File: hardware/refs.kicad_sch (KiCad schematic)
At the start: 26 parts, among them U4 LM4040DBZ-4.1, U5 OPA4991, U6 OPA4991

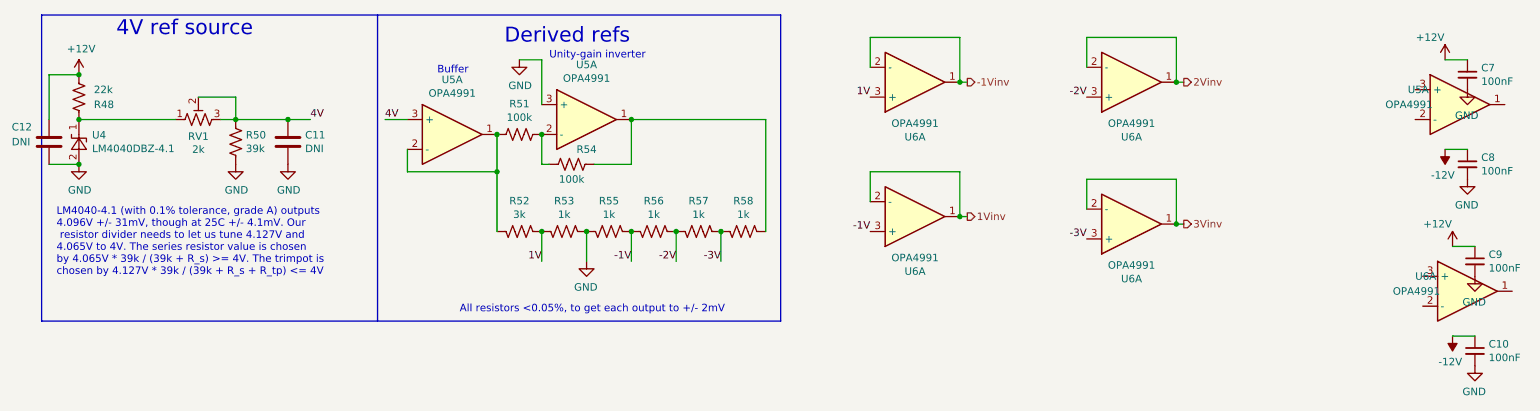
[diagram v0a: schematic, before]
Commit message: Fix 3d models and migrate to KiCad6 R/C footprints
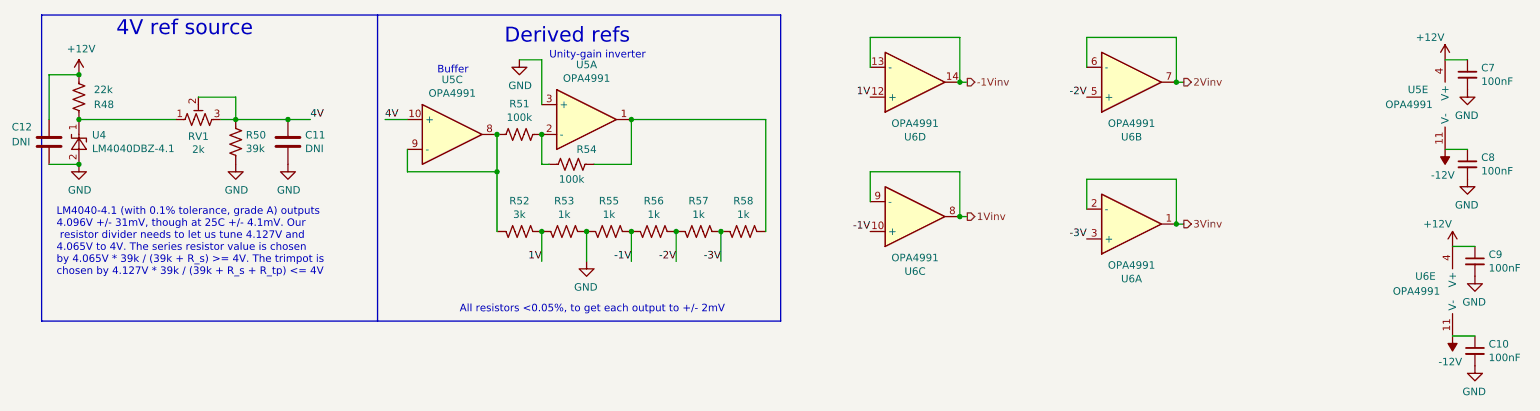
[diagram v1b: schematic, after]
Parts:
- C10, C11, C12, C7, C8, C9: footprint Capacitor_SMD:C_0603_1608Metric_Pad1.05x0.95mm_HandSolder -> Capacitor_SMD:C_0603_1608Metric_Pad1.08x0.95mm_HandSolder
- R48, R50, R51, R52, R53, R54, R55, R56, R57, R58: footprint Resistor_SMD:R_0603_1608Metric_Pad1.05x0.95mm_HandSolder -> Resistor_SMD:R_0603_1608Metric_Pad0.98x0.95mm_HandSolder
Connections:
- net +12V: now also U5.4 (V+), U6.4 (V+)
- net -12V: now also U5.11 (V-), U6.11 (V-)
- net -1V: now also U6.10 (+); no longer U6.3 (+)
- net -1Vinv: now also U6.13 (-), U6.14; no longer U6.1, U6.2 (-)
- net -2V: now also U6.5 (+); no longer U6.3 (+)
- net 1V: now also U6.12 (+); no longer U6.3 (+)
- net 1Vinv: now also U6.8, U6.9 (-); no longer U6.1, U6.2 (-)
- net 2Vinv: now also U6.6 (-), U6.7; no longer U6.1, U6.2 (-)
- net 4V: now also U5.10 (+); no longer U5.3 (+)
- net at R51.2, R52.1: now also U5.8, U5.9 (-); no longer U5.1, U5.2 (-)
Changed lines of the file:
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@@
     (effects (font (size 1.27 1.27)) (justify left))
   )
-  (symbol (lib_id "Device:Opamp_Quad_Generic") (at 91.44 36.83 0) (unit 1)
+  (symbol (lib_id "Device:Opamp_Quad_Generic") (at 91.44 36.83 0) (unit 3)
     (in_bom yes) (on_board yes)
     (property "Reference" "U5" (id 0) (at 91.44 27.5082 0))
@@
       (effects (font (size 1.27 1.27)) hide)
     )
-    (pin "1")
-    (pin "2")
-    (pin "3")
+    (pin "10")
+    (pin "8")
+    (pin "9")
   )
   (symbol (lib_id "Device:Opamp_Quad_Generic") (at 114.3 34.29 0) (unit 1)
@@
       (effects (font (size 1.27 1.27)) (justify left))
     )
-    (property "Footprint" "Resistor_SMD:R_0603_1608Metric_Pad1.05x0.95mm_HandSolder" (id 2) (at 55.626 38.354 90)
+    (property "Footprint" "Resistor_SMD:R_0603_1608Metric_Pad0.98x0.95mm_HandSolder" (id 2) (at 55.626 38.354 90)
       (effects (font (size 1.27 1.27)) hide)
     )
@@
     (property "Reference" "R51" (id 0) (at 102.87 31.623 90))
     (property "Value" "100k" (id 1) (at 102.87 33.9344 90))
-    (property "Footprint" "Resistor_SMD:R_0603_1608Metric_Pad1.05x0.95mm_HandSolder" (id 2) (at 102.616 37.846 90)
+    (property "Footprint" "Resistor_SMD:R_0603_1608Metric_Pad0.98x0.95mm_HandSolder" (id 2) (at 102.616 37.846 90)
       (effects (font (size 1.27 1.27)) hide)
     )
@@
     (property "Reference" "R54" (id 0) (at 114.3 39.37 90))
     (property "Value" "100k" (id 1) (at 111.76 44.45 90))
-    (property "Footprint" "Resistor_SMD:R_0603_1608Metric_Pad1.05x0.95mm_HandSolder" (id 2) (at 111.506 42.926 90)
+    (property "Footprint" "Resistor_SMD:R_0603_1608Metric_Pad0.98x0.95mm_HandSolder" (id 2) (at 111.506 42.926 90)
       (effects (font (size 1.27 1.27)) hide)
     )
@@
     (property "Reference" "R56" (id 0) (at 125.73 48.133 90))
     (property "Value" "1k" (id 1) (at 125.73 50.4444 90))
-    (property "Footprint" "Resistor_SMD:R_0603_1608Metric_Pad1.05x0.95mm_HandSolder" (id 2) (at 125.984 54.356 90)
+    (property "Footprint" "Resistor_SMD:R_0603_1608Metric_Pad0.98x0.95mm_HandSolder" (id 2) (at 125.984 54.356 90)
       (effects (font (size 1.27 1.27)) hide)
     )
@@
     (property "Reference" "R55" (id 0) (at 118.11 48.133 90))
     (property "Value" "1k" (id 1) (at 118.11 50.4444 90))
-    (property "Footprint" "Resistor_SMD:R_0603_1608Metric_Pad1.05x0.95mm_HandSolder" (id 2) (at 118.364 54.356 90)
+    (property "Footprint" "Resistor_SMD:R_0603_1608Metric_Pad0.98x0.95mm_HandSolder" (id 2) (at 118.364 54.356 90)
       (effects (font (size 1.27 1.27)) hide)
     )
@@
       (effects (font (size 1.27 1.27)) (justify left))
     )
-    (property "Footprint" "Resistor_SMD:R_0603_1608Metric_Pad1.05x0.95mm_HandSolder" (id 2) (at 28.956 30.734 90)
+    (property "Footprint" "Resistor_SMD:R_0603_1608Metric_Pad0.98x0.95mm_HandSolder" (id 2) (at 28.956 30.734 90)
       (effects (font (size 1.27 1.27)) hide)
     )
@@
     (property "Reference" "R57" (id 0) (at 133.35 48.133 90))
     (property "Value" "1k" (id 1) (at 133.35 50.4444 90))
-    (property "Footprint" "Resistor_SMD:R_0603_1608Metric_Pad1.05x0.95mm_HandSolder" (id 2) (at 133.604 54.356 90)
+    (property "Footprint" "Resistor_SMD:R_0603_1608Metric_Pad0.98x0.95mm_HandSolder" (id 2) (at 133.604 54.356 90)
       (effects (font (size 1.27 1.27)) hide)
     )
@@
     (property "Reference" "R53" (id 0) (at 110.49 48.133 90))
     (property "Value" "1k" (id 1) (at 110.49 50.4444 90))
-    (property "Footprint" "Resistor_SMD:R_0603_1608Metric_Pad1.05x0.95mm_HandSolder" (id 2) (at 110.744 54.356 90)
+    (property "Footprint" "Resistor_SMD:R_0603_1608Metric_Pad0.98x0.95mm_HandSolder" (id 2) (at 110.744 54.356 90)
       (effects (font (size 1.27 1.27)) hide)
     )
@@
     (property "Reference" "R52" (id 0) (at 102.87 48.133 90))
     (property "Value" "3k" (id 1) (at 102.87 50.4444 90))
-    (property "Footprint" "Resistor_SMD:R_0603_1608Metric_Pad1.05x0.95mm_HandSolder" (id 2) (at 103.124 54.356 90)
+    (property "Footprint" "Resistor_SMD:R_0603_1608Metric_Pad0.98x0.95mm_HandSolder" (id 2) (at 103.124 54.356 90)
       (effects (font (size 1.27 1.27)) hide)
     )
@@
     (property "Reference" "R58" (id 0) (at 140.97 48.133 90))
     (property "Value" "1k" (id 1) (at 140.97 50.4444 90))
-    (property "Footprint" "Resistor_SMD:R_0603_1608Metric_Pad1.05x0.95mm_HandSolder" (id 2) (at 141.224 54.356 90)
+    (property "Footprint" "Resistor_SMD:R_0603_1608Metric_Pad0.98x0.95mm_HandSolder" (id 2) (at 141.224 54.356 90)
       (effects (font (size 1.27 1.27)) hide)
     )
@@
     (pin "2")
   )
-  (symbol (lib_id "Device:Opamp_Quad_Generic") (at 170.18 27.94 0) (mirror x) (unit 1)
+  (symbol (lib_id "Device:Opamp_Quad_Generic") (at 170.18 27.94 0) (mirror x) (unit 4)
     (in_bom yes) (on_board yes)
     (property "Reference" "U6" (id 0) (at 170.18 37.2618 0))
@@
       (effects (font (size 1.27 1.27)) hide)
     )
-    (pin "1")
-    (pin "2")
-    (pin "3")
-  )
-  (symbol (lib_id "Device:Opamp_Quad_Generic") (at 170.18 50.8 0) (mirror x) (unit 1)
+    (pin "12")
+    (pin "13")
+    (pin "14")
+  )
+  (symbol (lib_id "Device:Opamp_Quad_Generic") (at 170.18 50.8 0) (mirror x) (unit 3)
     (in_bom yes) (on_board yes)
     (property "Reference" "U6" (id 0) (at 170.18 60.1218 0))
@@
       (effects (font (size 1.27 1.27)) hide)
     )
-    (pin "1")
-    (pin "2")
-    (pin "3")
-  )
-  (symbol (lib_id "Device:Opamp_Quad_Generic") (at 207.01 27.94 0) (mirror x) (unit 1)
+    (pin "10")
+    (pin "8")
+    (pin "9")
+  )
+  (symbol (lib_id "Device:Opamp_Quad_Generic") (at 207.01 27.94 0) (mirror x) (unit 2)
     (in_bom yes) (on_board yes)
     (property "Reference" "U6" (id 0) (at 207.01 37.2618 0))
@@
       (effects (font (size 1.27 1.27)) hide)
     )
-    (pin "1")
-    (pin "2")
-    (pin "3")
+    (pin "5")
+    (pin "6")
+    (pin "7")
   )
   (symbol (lib_id "Device:Opamp_Quad_Generic") (at 207.01 52.07 0) (mirror x) (unit 1)
@@
     (pin "3")
   )
-  (symbol (lib_id "Device:Opamp_Quad_Generic") (at 262.89 31.75 0) (unit 1)
+  (symbol (lib_id "Device:Opamp_Quad_Generic") (at 262.89 31.75 0) (unit 5)
     (in_bom yes) (on_board yes)
     (property "Reference" "U5" (id 0) (at 254 29.21 0)
@@
       (effects (font (size 1.27 1.27)) hide)
     )
-    (pin "1")
-    (pin "2")
-    (pin "3")
+    (pin "11")
+    (pin "4")
   )
   (symbol (lib_id "Device:C_Small") (at 264.16 26.67 0) (unit 1)
@@
       (effects (font (size 1.27 1.27)) (justify left))
     )
-    (property "Footprint" "Capacitor_SMD:C_0603_1608Metric_Pad1.05x0.95mm_HandSolder" (id 2) (at 264.16 26.67 0)
+    (property "Footprint" "Capacitor_SMD:C_0603_1608Metric_Pad1.08x0.95mm_HandSolder" (id 2) (at 264.16 26.67 0)
       (effects (font (size 1.27 1.27)) hide)
     )
@@
       (effects (font (size 1.27 1.27)) (justify left))
     )
-    (property "Footprint" "Capacitor_SMD:C_0603_1608Metric_Pad1.05x0.95mm_HandSolder" (id 2) (at 264.16 41.91 0)
+    (property "Footprint" "Capacitor_SMD:C_0603_1608Metric_Pad1.08x0.95mm_HandSolder" (id 2) (at 264.16 41.91 0)
       (effects (font (size 1.27 1.27)) hide)
     )
@@
     (pin "1")
   )
-  (symbol (lib_id "Device:Opamp_Quad_Generic") (at 264.16 63.5 0) (unit 1)
+  (symbol (lib_id "Device:Opamp_Quad_Generic") (at 264.16 63.5 0) (unit 5)
     (in_bom yes) (on_board yes)
     (property "Reference" "U6" (id 0) (at 255.27 60.96 0)
@@
       (effects (font (size 1.27 1.27)) hide)
     )
-    (pin "1")
-    (pin "2")
-    (pin "3")
+    (pin "11")
+    (pin "4")
   )
   (symbol (lib_id "Device:C_Small") (at 265.43 58.42 0) (unit 1)
@@
       (effects (font (size 1.27 1.27)) (justify left))
     )
-    (property "Footprint" "Capacitor_SMD:C_0603_1608Metric_Pad1.05x0.95mm_HandSolder" (id 2) (at 265.43 58.42 0)
+    (property "Footprint" "Capacitor_SMD:C_0603_1608Metric_Pad1.08x0.95mm_HandSolder" (id 2) (at 265.43 58.42 0)
       (effects (font (size 1.27 1.27)) hide)
     )
@@
       (effects (font (size 1.27 1.27)) (justify left))
     )
-    (property "Footprint" "Capacitor_SMD:C_0603_1608Metric_Pad1.05x0.95mm_HandSolder" (id 2) (at 265.43 73.66 0)
+    (property "Footprint" "Capacitor_SMD:C_0603_1608Metric_Pad1.08x0.95mm_HandSolder" (id 2) (at 265.43 73.66 0)
       (effects (font (size 1.27 1.27)) hide)
     )
@@
       (effects (font (size 1.27 1.27)) (justify left))
     )
-    (property "Footprint" "Capacitor_SMD:C_0603_1608Metric_Pad1.05x0.95mm_HandSolder" (id 2) (at 64.4652 41.91 0)
+    (property "Footprint" "Capacitor_SMD:C_0603_1608Metric_Pad1.08x0.95mm_HandSolder" (id 2) (at 64.4652 41.91 0)
       (effects (font (size 1.27 1.27)) hide)
     )
@@
       (effects (font (size 1.27 1.27)) (justify left))
     )
-    (property "Footprint" "Capacitor_SMD:C_0603_1608Metric_Pad1.05x0.95mm_HandSolder" (id 2) (at 23.8252 41.91 0)
-      (effects (font (size 1.27 1.27)) hide)
-    )
+    (property "Footprint" "Capacitor_SMD:C_0603_1608Metric_Pad1.08x0.95mm_HandSolder" (id 2) (at 23.8252 41.91 0)
+      (effects (font (size 1.27 1.27)) hide)
+    )
